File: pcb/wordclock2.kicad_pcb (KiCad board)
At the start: 2 copper layers, 130 x 30 mm, 58 parts, among them J1 Jack-DC, J2 CONN_02X05, J3 Micro_SD_Card_Det, J4 USB_OTG, J5 CONN_01X03, J6 CONN_01X03, Q1 FDS6890A, SW1 SW_Push, SW2 SW_Push, SW3 SW_Push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

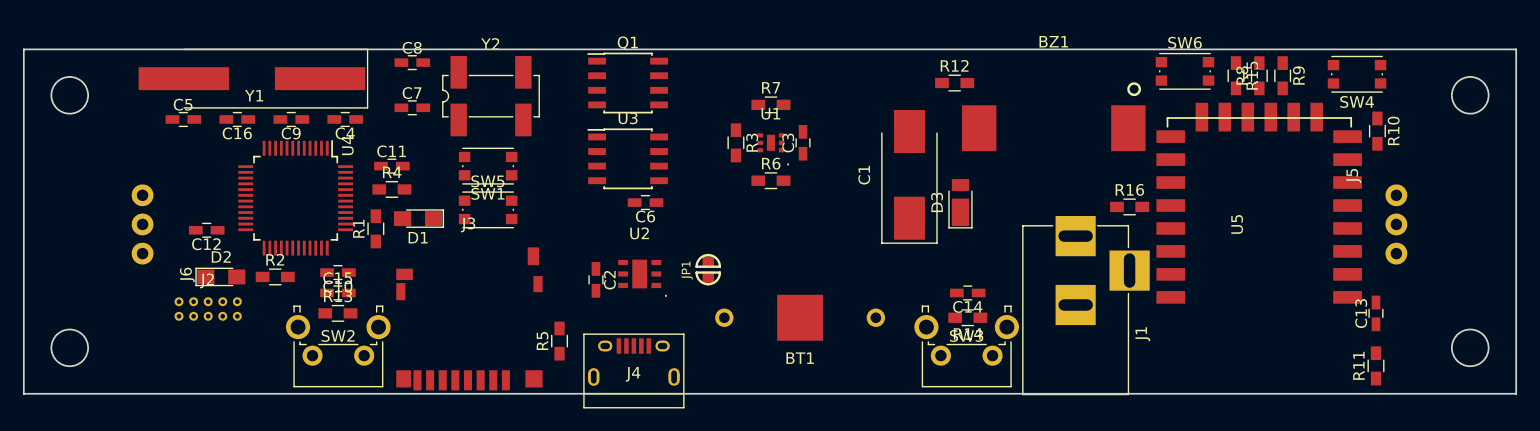
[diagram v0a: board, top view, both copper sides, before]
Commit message: updated sd-card detection pad
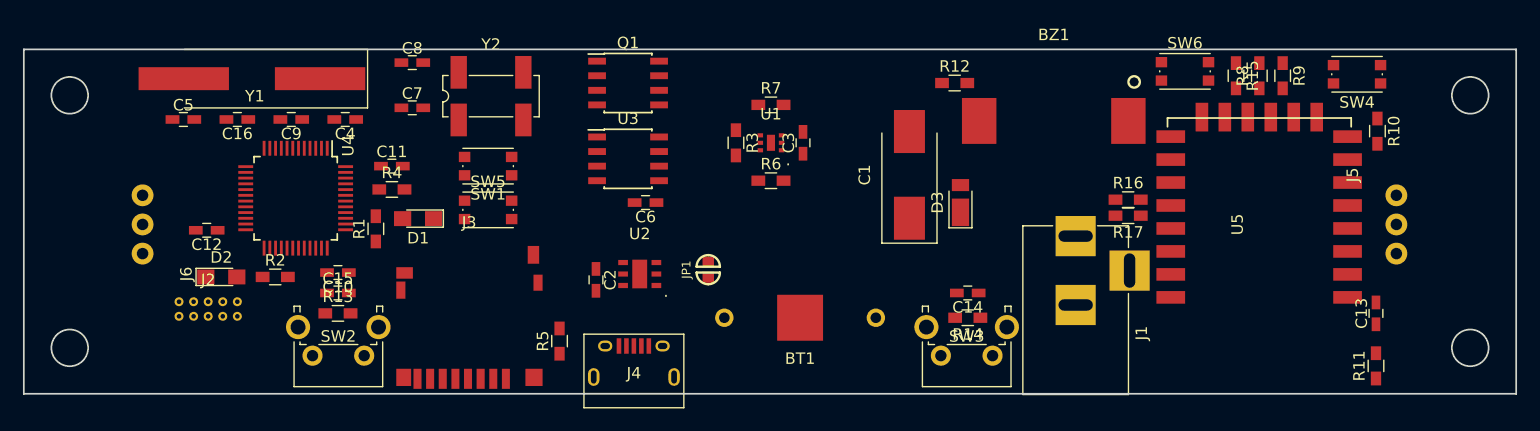
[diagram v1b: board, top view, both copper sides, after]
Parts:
- added R17: 100, Resistors_SMD:R_0603_HandSoldering, F.Cu at (179.2, 94.5)
- J3: value Micro_SD_Card_Det -> Micro_SD_HIROSE
- moved R16 0.65 mm to (179.2, 93.1)
- moved BZ1 0.63 mm to (172.7, 86.2)
- moved J3 0.13 mm to (121.8, 107.8)
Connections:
- J3 pad A: (no net) -> /SD_DET
- J3 pad B: (no net) -> GND
- SW5 pad 1: GND -> +3V3
- U5 pad 13: /BOOT0 -> Net-(R17-Pad1)

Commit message: first tracks
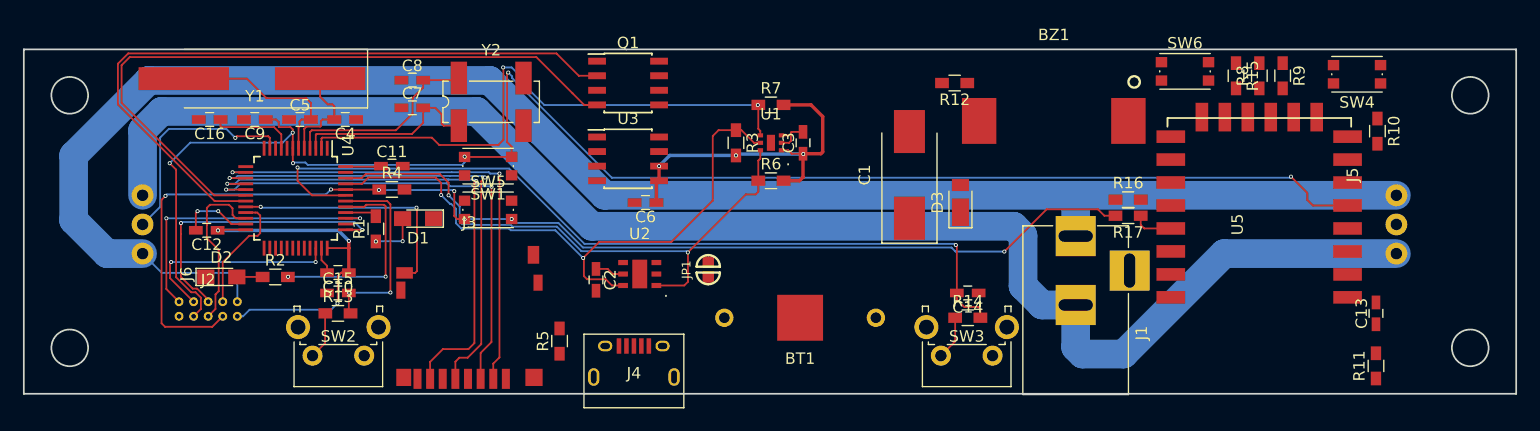
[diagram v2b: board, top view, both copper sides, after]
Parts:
- moved C5 10.2 mm to (107.1, 86.1)
- moved C9 3.18 mm to (103.1, 86.1)
- moved C16 2.41 mm to (99.2, 86.1)
- moved C8 1.52 mm to (116.8, 82.7)
- moved Y2 0.50 mm to (123.7, 84.6)
- turned R12 to 180 degrees
- turned R14 to 0 degrees
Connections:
- J3 pad A: /SD_DET -> GND
- J3 pad B: GND -> /SD_DET
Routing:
- net +5V: track 0.00 -> 149.8 mm
- net GND: track 0.00 -> 144.9 mm, vias 0 -> 2
- net /ST_NRST: track 0.00 -> 137.7 mm, vias 0 -> 6
- net /BOOT0: track 0.00 -> 105.5 mm, vias 0 -> 7
- net +3V3: track 0.00 -> 75.5 mm, vias 0 -> 6
- net /USER_BTN2: track 0.00 -> 74.0 mm, vias 0 -> 2
- net /BUZZ_EN: track 0.00 -> 61.1 mm
- net /SD_EN: track 0.00 -> 60.9 mm
- net /I2C_SCL: track 0.00 -> 54.3 mm, vias 0 -> 2
- net /I2C_SDA: track 0.00 -> 51.7 mm, vias 0 -> 2
- net /I2C_INT: track 0.00 -> 50.1 mm, vias 0 -> 2
- net /SPI_MISO: track 0.00 -> 43.9 mm, vias 0 -> 2
- net /SPI_SCK: track 0.00 -> 42.9 mm, vias 0 -> 2
- net /SD_CS: track 0.00 -> 42.6 mm, vias 0 -> 2
- net /SPI_MOSI: track 0.00 -> 42.3 mm, vias 0 -> 2
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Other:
- net class Default: clearance 0.2 -> 0.16; trace_width 0.25 -> 0.16; via_dia 0.6 -> 0.35; via_drill 0.4 -> 0.2
- net class PowerHigh added: clearance 0.2, trace_width 2.5, via_dia 2.5, via_drill 1.5
- net class PowerLow added: clearance 0.16, trace_width 0.3, via_dia 0.35, via_drill 0.2
- rule trace_clearance: 0.2 -> 0.16
- rule trace_min: 0.2 -> 0.16
- rule via_min_drill: 0.3 -> 0.1
- rule via_min_size: 0.4 -> 0.2

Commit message: ESD Diodes USB, many tracks, huge progress
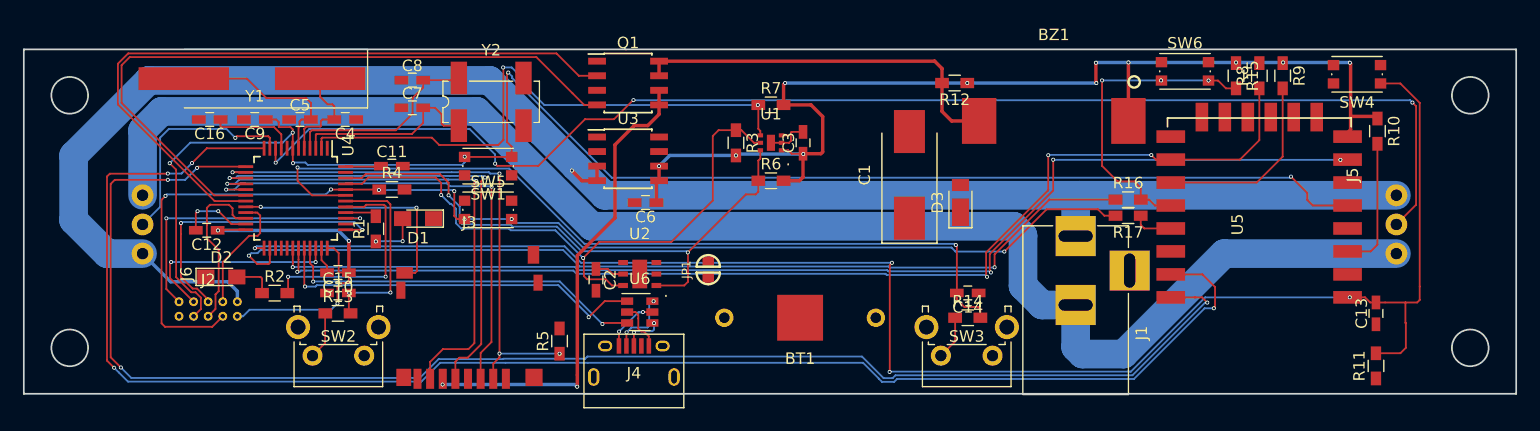
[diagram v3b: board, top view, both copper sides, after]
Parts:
- added U6: USBLC6-2SC6, TO_SOT_Packages_SMD:SOT-23-6, F.Cu at (136.7, 102.9)
- moved R2 1.41 mm to (104.9, 101.2)
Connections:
- J4 pad 2: /USB_DM -> Net-(J4-Pad2)
- J4 pad 3: /USB_DP -> Net-(J4-Pad3)
- U4 pad 38: /PA15 -> Net-(U4-Pad38)
- U5 pad 14: /PA15 -> Net-(U5-Pad14)
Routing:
- net /ESP_RST: track 0.00 -> 145.5 mm, vias 0 -> 4
- net /UART_WLAN_TX: track 0.00 -> 137.4 mm, vias 0 -> 4
- net /UART_WLAN_RX: track 0.00 -> 130.8 mm, vias 0 -> 4
- net /LEDStripe1: track 0.00 -> 117.2 mm, vias 0 -> 4
- net /UART_OTA_TX: track 0.00 -> 99.9 mm, vias 0 -> 4
- net /UART_OTA_RX: track 0.00 -> 99.1 mm, vias 0 -> 4
- net Net-(R16-Pad1): track 0.00 -> 82.9 mm, vias 0 -> 2
- net +3V3: track 75.5 -> 145.5 mm, vias 6 -> 14
- net Net-(J3-Pad6): track 0.00 -> 41.8 mm, vias 0 -> 2
- net Net-(BZ1-Pad1): track 0.00 -> 33.5 mm
- net /USB_DM: track 0.00 -> 33.3 mm, vias 0 -> 2
- net /USB_DP: track 0.00 -> 32.0 mm, vias 0 -> 2
- net /ESP_GPIO0: track 0.00 -> 28.2 mm, vias 0 -> 3
- net Net-(R9-Pad2): track 0.00 -> 15.9 mm
- net Net-(R10-Pad2): track 0.00 -> 12.3 mm
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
